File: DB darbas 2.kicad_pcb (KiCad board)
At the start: 2 copper layers, 68.8 x 53.6 mm, 18 parts, among them J1 XLR3_Ground, J3 XLR3_Ground, U1 Arduino_UNO_R2

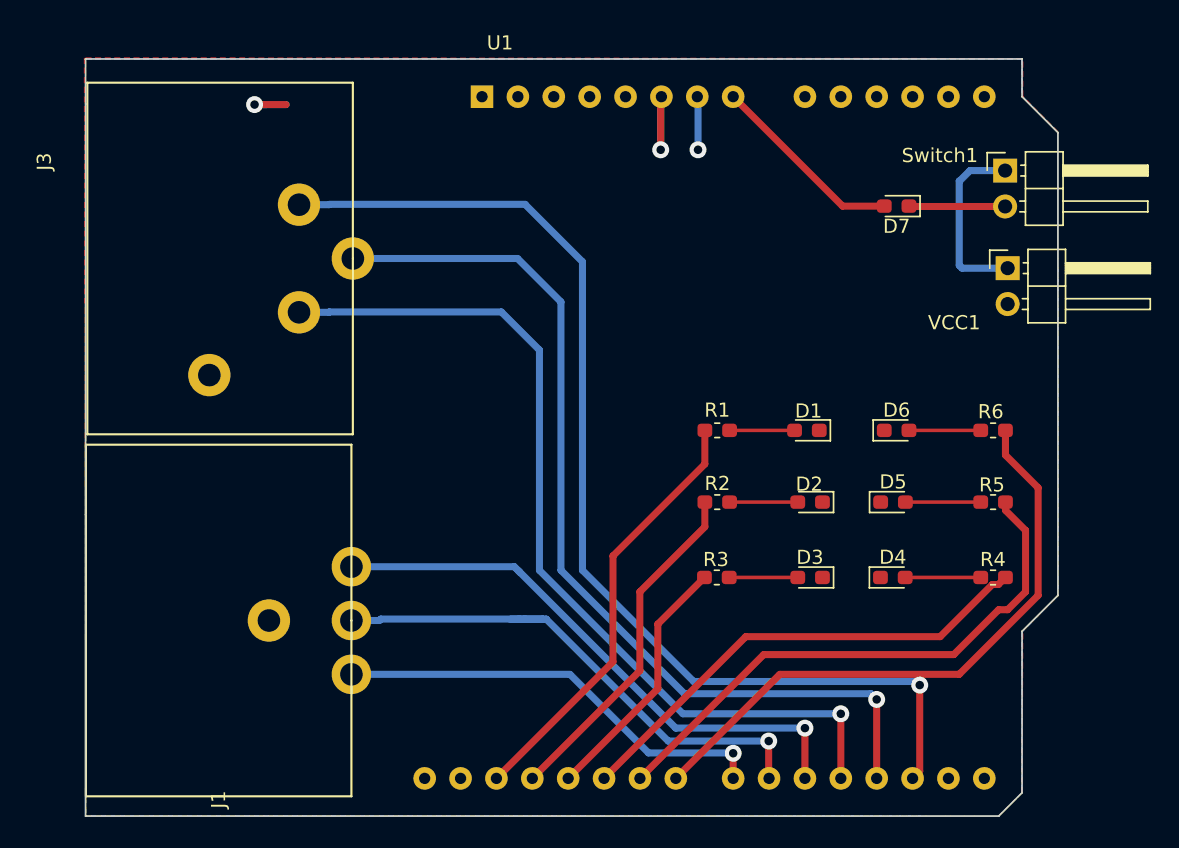
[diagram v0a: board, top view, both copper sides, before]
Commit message: DMX laidų testeris REV 1.2
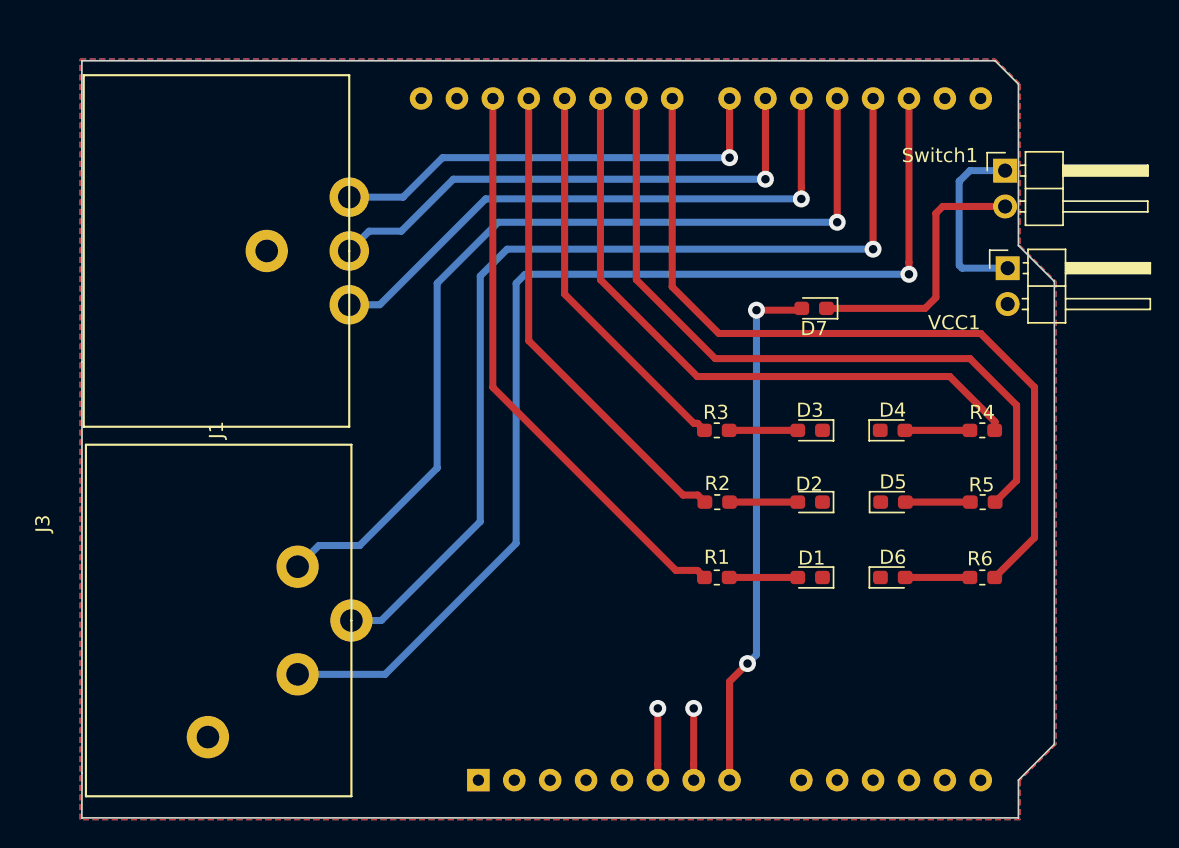
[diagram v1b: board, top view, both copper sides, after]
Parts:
- U1: moved to B.Cu
- moved U1 48.4 mm to (108.0, 125.1)
- moved J1 26.2 mm to (98.8, 87.6)
- moved J3 25.6 mm to (99.0, 113.8)
- moved R4 10.4 mm to (143.6, 100.3)
- moved R6 10.4 mm to (143.6, 110.7)
- moved D6 10.4 mm to (137.3, 110.7)
- moved D1 10.4 mm to (131.4, 110.7)
- moved R1 10.4 mm to (124.8, 110.7)
- moved D4 10.4 mm to (137.3, 100.3)
- moved D3 10.4 mm to (131.4, 100.3)
- moved R3 10.4 mm to (124.8, 100.3)
- moved D7 9.30 mm to (131.7, 91.7)
- moved R5 0.73 mm to (143.7, 105.4)
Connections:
- U1 pad 17: Net-(J3-Pad2) -> Net-(J3-Pad1)
- U1 pad 19: Net-(J3-Pad1) -> Net-(J3-Pad2)
- U1 pad 20: Net-(J1-Pad1) -> Net-(J1-Pad2)
- U1 pad 22: Net-(J1-Pad2) -> Net-(J1-Pad1)
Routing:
- net Net-(D7-Pad2): track 13.9 -> 37.3 mm, vias 0 -> 2
- net Net-(J3-Pad1): track 63.9 -> 78.2 mm
- net Net-(J3-Pad2): track 78.0 -> 64.7 mm
- net Net-(R6-Pad2): track 43.7 -> 56.6 mm
- net Net-(D7-Pad1): track 6.82 -> 19.1 mm
- net Net-(R4-Pad2): track 34.3 -> 45.5 mm
- net Net-(R5-Pad2): track 39.7 -> 50.9 mm
- net Net-(J1-Pad2): track 31.1 -> 42.2 mm
- net Net-(R1-Pad1): track 30.8 -> 41.0 mm
- net Net-(R2-Pad2): track 24.6 -> 34.4 mm
- net Net-(R3-Pad2): track 18.2 -> 27.7 mm
- net Net-(J1-Pad1): track 40.6 -> 32.3 mm
- net GND: track 17.2 -> 10.2 mm, vias 3 -> 2
- net Net-(J3-Pad3): track 66.7 -> 68.7 mm
- net Net-(D4-Pad2): track 5.35 -> 4.60 mm
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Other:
- outline, holes or cut-outs redrawn

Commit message: Ver1.3
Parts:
- moved VCC1 28.5 mm to (144.8, 117.3)
- moved Switch1 3.00 mm to (142.2, 81.8)
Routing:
- net Net-(Switch1-Pad1): track 13.0 -> 41.7 mm
- net Net-(D7-Pad1): track 19.1 -> 16.9 mm
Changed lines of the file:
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@@
     (thickness 1.6)
     (drawings 2)
-    (tracks 105)
+    (tracks 102)
     (zones 0)
     (modules 18)
@@
     (pcbplotparams
       (layerselection 0x01000_ffffffff)
-      (usegerberextensions true)
+      (usegerberextensions false)
       (usegerberattributes false)
       (usegerberadvancedattributes false)
@@
       (psnegative false)
       (psa4output false)
-      (plotreference true)
-      (plotvalue true)
+      (plotreference false)
+      (plotvalue false)
       (plotinvisibletext false)
-      (padsonsilk false)
+      (padsonsilk true)
       (subtractmaskfromsilk false)
       (outputformat 1)
@@
       (effects (font (size 1 1) (thickness 0.15)))
     )
-    (fp_text value XLR3_Ground (at -6.096 -21.59 90) (layer F.Fab)
+    (fp_text value XLR3_Ground (at 0.762 -11.3284 90) (layer F.Fab)
       (effects (font (size 1 1) (thickness 0.15)))
     )
@@
   )
   (module Connector_PinHeader_2.54mm:PinHeader_1x02_P2.54mm_Horizontal (layer F.Cu)
-    (at 145.415 88.847801)
+    (at 144.78 117.348)
     (descr "Through hole angled pin header, 1x02, 2.54mm pitch, 6mm pin length, single row")
     (tags "Through hole angled pin header THT 1x02 2.54mm single row")
@@
   )
   (module Connector_PinHeader_2.54mm:PinHeader_1x02_P2.54mm_Horizontal (layer F.Cu)
-    (at 145.2372 81.9404)
+    (at 142.24 81.788)
     (descr "Through hole angled pin header, 1x02, 2.54mm pitch, 6mm pin length, single row")
     (tags "Through hole angled pin header THT 1x02 2.54mm single row")
@@
   (segment (start 138.43 88.432472) (end 138.43 76.835) (width 0.5) (layer F.Cu) (net 34))
   (segment (start 138.43 89.281) (end 138.43 88.432472) (width 0.5) (layer F.Cu) (net 34))
-  (segment (start 142.187801 88.847801) (end 145.415 88.847801) (width 0.5) (layer B.Cu) (net 35))
-  (segment (start 141.986 88.646) (end 142.187801 88.847801) (width 0.5) (layer B.Cu) (net 35))
-  (segment (start 142.0114 82.677) (end 142.748 81.9404) (width 0.5) (layer B.Cu) (net 35))
-  (segment (start 141.986 82.677) (end 142.0114 82.677) (width 0.5) (layer B.Cu) (net 35))
-  (segment (start 145.2372 81.9404) (end 142.748 81.9404) (width 0.5) (layer B.Cu) (net 35))
-  (segment (start 141.986 82.677) (end 141.986 88.646) (width 0.5) (layer B.Cu) (net 35))
+  (segment (start 142.24 81.788) (end 140.716 81.788) (width 0.5) (layer B.Cu) (net 35))
+  (segment (start 139.719999 82.784001) (end 139.719999 115.843999) (width 0.5) (layer B.Cu) (net 35))
+  (segment (start 140.716 81.788) (end 139.719999 82.784001) (width 0.5) (layer B.Cu) (net 35))
+  (segment (start 141.224 117.348) (end 144.78 117.348) (width 0.5) (layer B.Cu) (net 35))
+  (segment (start 139.719999 115.843999) (end 141.224 117.348) (width 0.5) (layer B.Cu) (net 35))
   (via (at 127 116.84) (size 1.2) (drill 0.6) (layers F.Cu B.Cu) (net 36))
   (segment (start 125.73 125.095) (end 125.73 118.11) (width 0.5) (layer F.Cu) (net 36))
@@
   (segment (start 130.711 91.821) (end 130.838 91.694) (width 0.5) (layer F.Cu) (net 36))
   (segment (start 127.635 91.821) (end 130.711 91.821) (width 0.5) (layer F.Cu) (net 36))
-  (segment (start 132.588 91.694) (end 139.573 91.694) (width 0.5) (layer F.Cu) (net 37))
-  (segment (start 139.573 91.694) (end 140.335 90.932) (width 0.5) (layer F.Cu) (net 37))
-  (segment (start 140.335 90.932) (end 140.335 84.963) (width 0.5) (layer F.Cu) (net 37))
-  (segment (start 140.8176 84.4804) (end 145.2372 84.4804) (width 0.5) (layer F.Cu) (net 37))
-  (segment (start 140.335 84.963) (end 140.8176 84.4804) (width 0.5) (layer F.Cu) (net 37))
+  (segment (start 142.24 91.44) (end 142.24 84.328) (width 0.5) (layer F.Cu) (net 37))
+  (segment (start 132.588 91.694) (end 141.986 91.694) (width 0.5) (layer F.Cu) (net 37))
+  (segment (start 141.986 91.694) (end 142.24 91.44) (width 0.5) (layer F.Cu) (net 37))
   (zone (net 31) (net_name GND) (layer B.Cu) (hatch edge 0.508)
     (connect_pads (clearance 0.508))
